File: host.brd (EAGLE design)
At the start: 82.5 x 43.3 mm, 106 parts, among them IC1 74LVC1T45GS,132, IC10 74LVC1T45GS,132, IC11 74LVC1T45GS,132, IC2 NCP187AMT120TAG, IC3 LD39200PU33R, IC4 74LVC1T45GS,132, IC5 74LVC1T45GS,132, IC6 74LVC1T45GS,132, IC7 74ALVC164245DGG:11, IC8 74ALVC164245DGG:11, IC9 74LVC1T45GS,132, Y1 DSC6001J

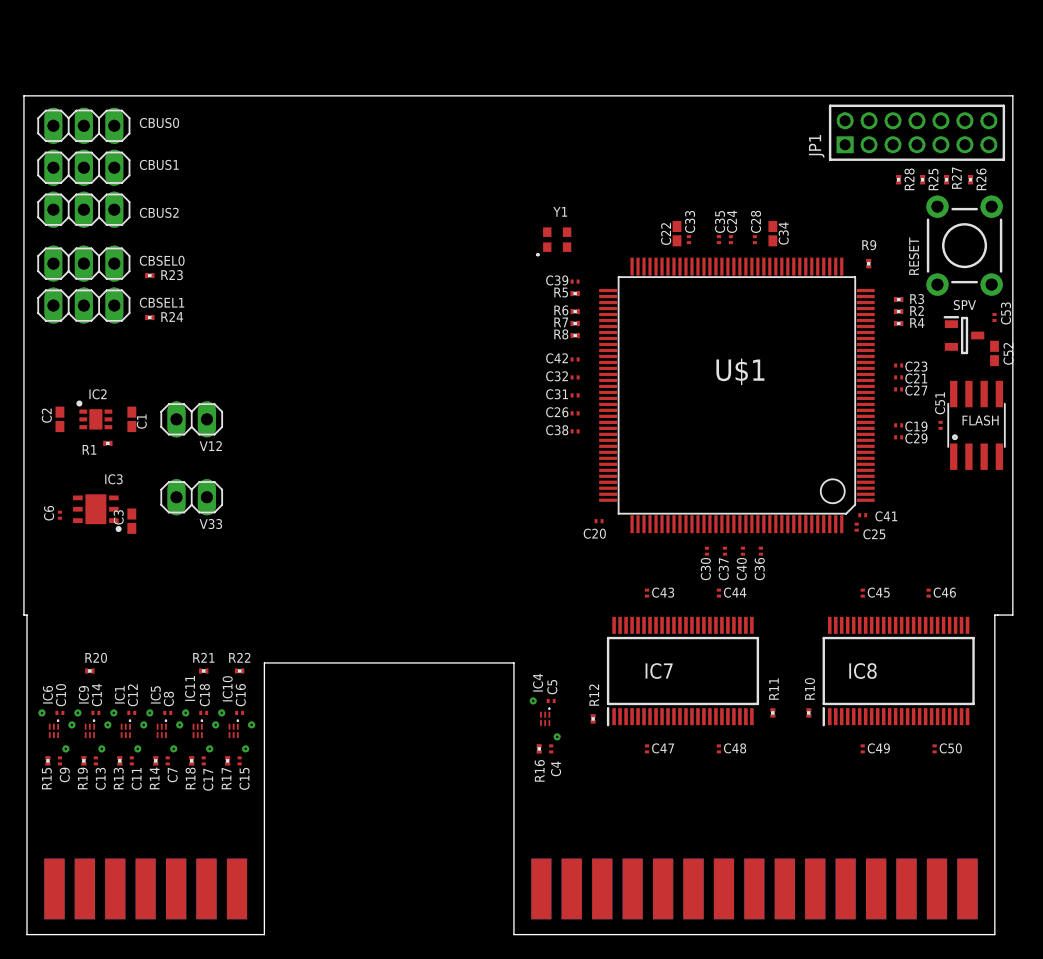
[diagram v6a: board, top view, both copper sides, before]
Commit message: Move to micro-HDMI for the interconnect cable
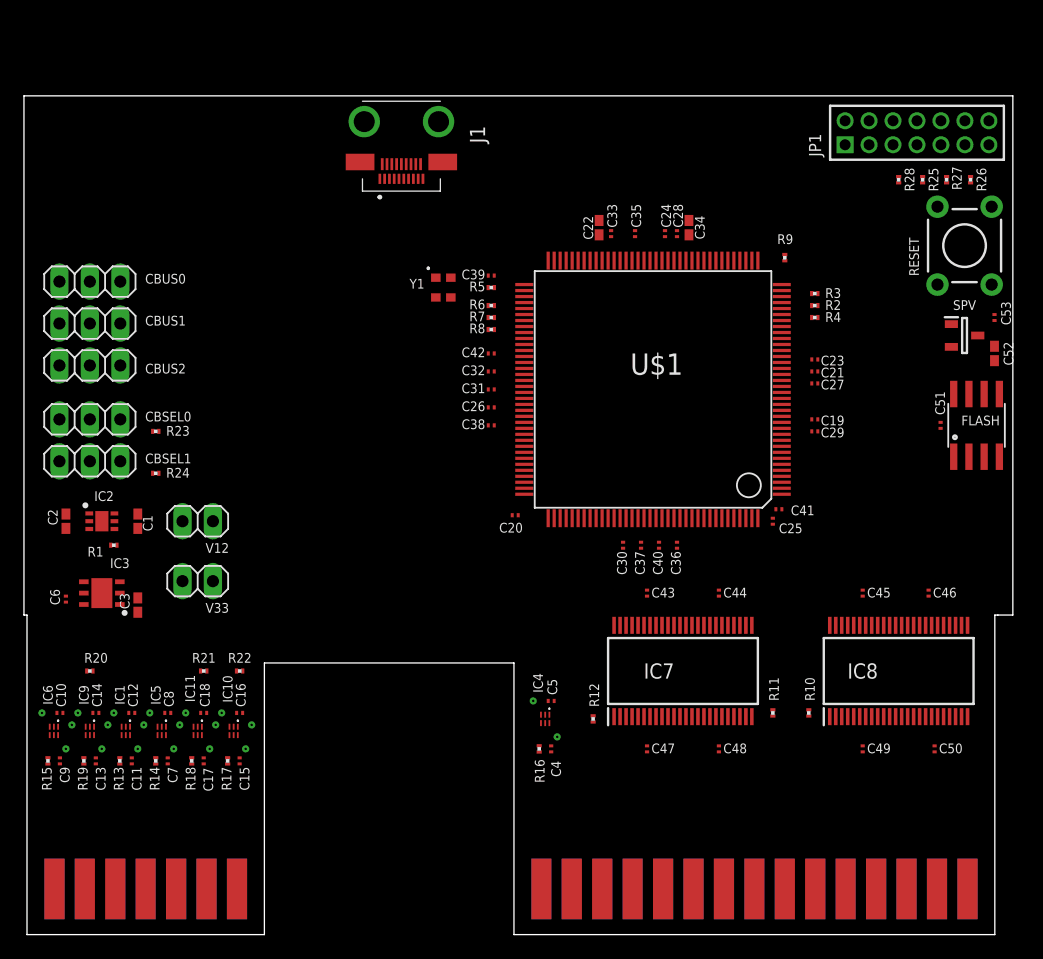
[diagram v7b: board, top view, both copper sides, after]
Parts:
- added J1: 10118241-001RLF, host:10118241001RLF
- moved CBSEL0 13.0 mm to (5.50, 43.0)
- moved CBSEL1 13.0 mm to (5.50, 39.5)
- moved CBUS0 13.0 mm to (5.50, 54.5)
- moved CBUS1 13.0 mm to (5.50, 51.0)
- moved CBUS2 13.0 mm to (5.50, 47.5)
- moved R23 13.0 mm to (11.0, 42.0)
- moved R24 13.0 mm to (11.0, 38.5)
- moved Y1 10.3 mm to (35.0, 54.0), turned to 270 degrees
- moved C1 8.51 mm to (9.50, 34.5)
- moved C2 8.51 mm to (3.50, 34.5)
- moved IC2 8.51 mm to (6.50, 34.5)
- moved R1 8.51 mm to (7.50, 32.5)
- moved V12 8.51 mm to (14.5, 34.5)
- moved C19 7.02 mm to (66.0, 43.0)
- moved C20 7.02 mm to (41.0, 35.0)
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
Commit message: Add in the debug headers
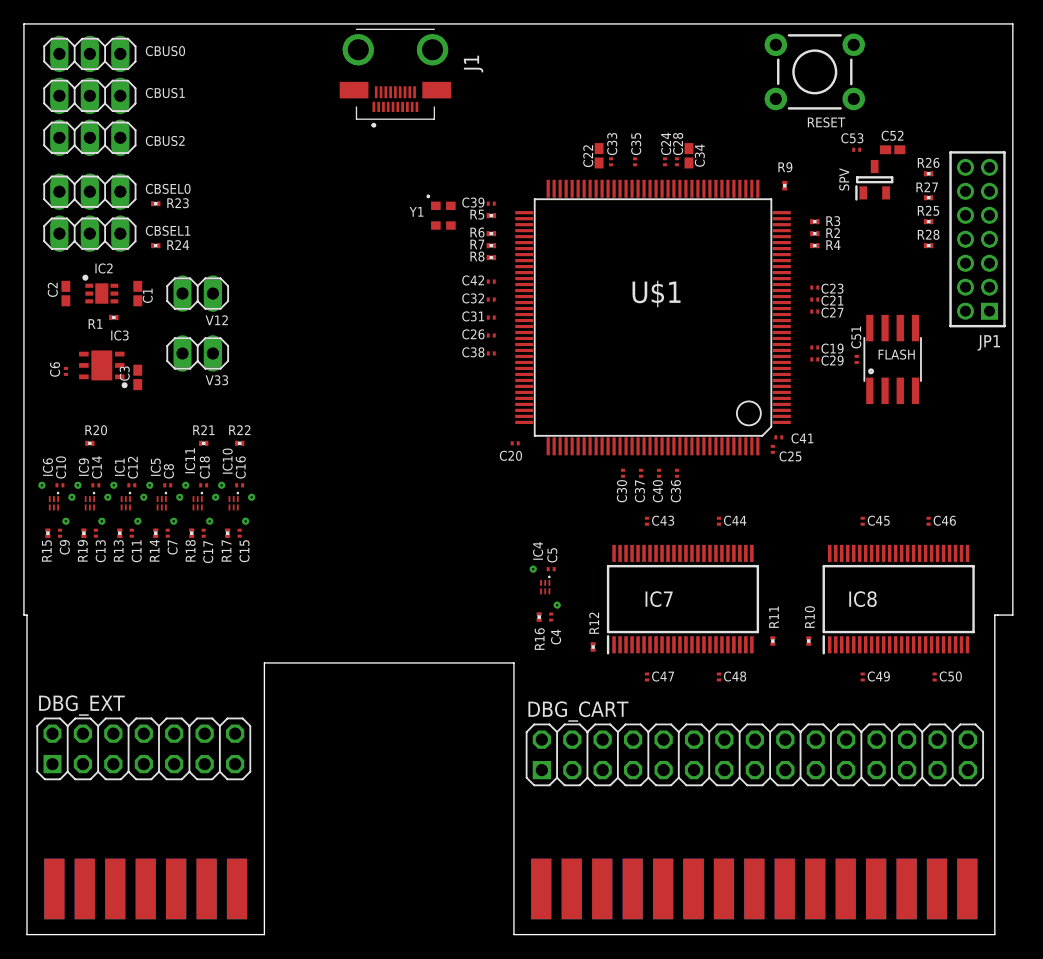
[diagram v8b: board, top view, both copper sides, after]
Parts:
- added DBG_CART: (no value), pinhead-2:2X15
- added DBG_EXT: (no value), pinhead-2:2X07
- moved RESET 19.1 mm to (66.0, 72.0), turned to 180 degrees
- moved C52 19.0 mm to (72.5, 65.5), turned to 0 degrees
- moved C1 19.0 mm to (9.50, 53.5)
- moved C10 19.0 mm to (3.00, 37.5)
- moved C11 19.0 mm to (9.00, 33.5)
- moved C12 19.0 mm to (9.00, 37.5)
- moved C13 19.0 mm to (6.00, 33.5)
- moved C14 19.0 mm to (6.00, 37.5)
- moved C15 19.0 mm to (18.0, 33.5)
- moved C16 19.0 mm to (18.0, 37.5)
- moved C17 19.0 mm to (15.0, 33.5)
- moved C18 19.0 mm to (15.0, 37.5)
- moved C2 19.0 mm to (3.50, 53.5)
- moved C3 19.0 mm to (9.50, 46.5)
- moved C6 19.0 mm to (3.50, 47.0)
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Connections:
- new net AUDIO: DBG_EXT.5, U$2.E5
- new net RSRVD: DBG_EXT.14, U$2.E:A
- net !A8_CCTL!: now also DBG_CART.1
- net !A8_CLK!: now also DBG_CART.2
- net !A8_D1XX!: now also DBG_EXT.9
- net !A8_EXTSEL!: now also DBG_EXT.13
- net !A8_HALT!: now also DBG_EXT.10
- net !A8_IRQ!: now also DBG_EXT.12
- net !A8_MPD!: now also DBG_EXT.7
- net !A8_REF!: now also DBG_EXT.3
- net !A8_RESET!: now also DBG_EXT.11
- net !A8_S4!: now also DBG_CART.29
- net !A8_S5!: now also DBG_CART.7
- net +5V: now also DBG_CART.5, DBG_EXT.1
- net A8_A0: now also DBG_CART.21
- net A8_A1: now also DBG_CART.23
- net A8_A10: now also DBG_CART.6
- net A8_A11: now also DBG_CART.8
- net A8_A12: now also DBG_CART.14
- net A8_A13: now also DBG_EXT.8
- net A8_A14: now also DBG_EXT.6
- net A8_A15: now also DBG_EXT.4
- net A8_A2: now also DBG_CART.25
- net A8_A3: now also DBG_CART.27
- net A8_A4: now also DBG_CART.26
- net A8_A5: now also DBG_CART.24
- net A8_A6: now also DBG_CART.22
- net A8_A7: now also DBG_CART.20
- net A8_A8: now also DBG_CART.18
- net A8_A9: now also DBG_CART.16
- net A8_D0: now also DBG_CART.11
- net A8_D1: now also DBG_CART.13
- net A8_D2: now also DBG_CART.15
- net A8_D3: now also DBG_CART.12
- net A8_D4: now also DBG_CART.19
- net A8_D5: now also DBG_CART.17
- net A8_D6: now also DBG_CART.9
- net A8_D7: now also DBG_CART.10
- net A8_R/!W!: now also DBG_CART.4
- net A8_RD4: now also DBG_CART.30
- net A8_RD5: now also DBG_CART.3
- net GND: now also DBG_CART.28, DBG_EXT.2
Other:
- board size 82.5 x 43.3 mm -> 82.5 x 49.3 mm
